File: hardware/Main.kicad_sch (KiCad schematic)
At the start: 16 parts, among them SW1 Bourns PEC11R, SW2 Bourns PEC11R, U3 RPi_Pico_TH

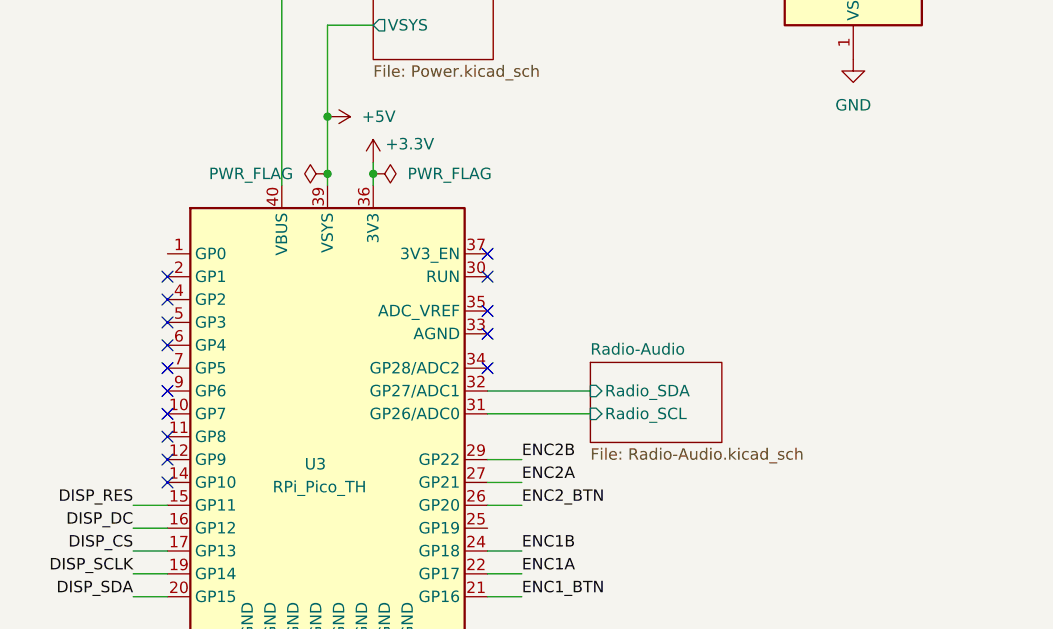
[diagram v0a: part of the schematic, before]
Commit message: PWM Audio, Power fix
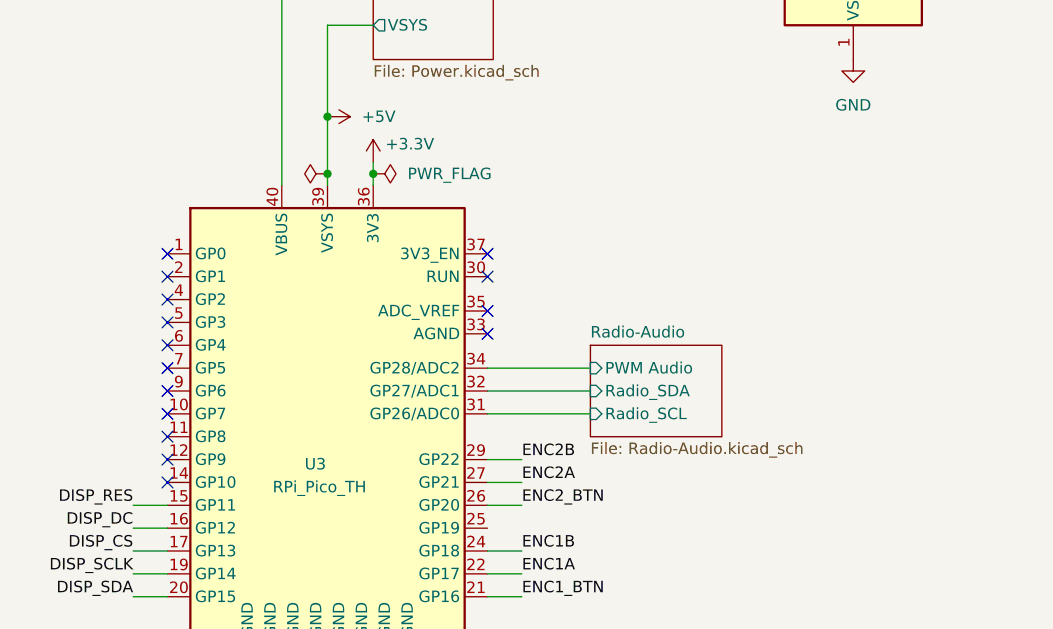
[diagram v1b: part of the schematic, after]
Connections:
- net Radio-Audio/PWM Audio: now reaches U3.34 (GP28/ADC2)
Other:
- sheet Radio-Audio ports: added PWM Audio; removed none
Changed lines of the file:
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@@
 	)
 	(no_connect
+		(at 105.41 78.74)
+	)
+	(no_connect
 		(at 105.41 99.06)
 	)
@@
 	)
 	(no_connect
-		(at 140.97 91.44)
-	)
-	(no_connect
 		(at 140.97 81.28)
 	)
@@
 	(wire
 		(pts
+			(xy 140.97 91.44) (xy 152.4 91.44)
+		)
+		(stroke
+			(width 0)
+			(type default)
+		)
+	)
+	(wire
+		(pts
 			(xy 54.61 69.85) (xy 54.61 73.66)
 		)
@@
 		(on_board yes)
 		(dnp no)
-		(fields_autoplaced yes)
 		(property "Reference" "#FLG01"
 			(at 121.285 69.85 0)
@@
 		)
 		(property "Value" "PWR_FLAG"
-			(at 119.38 69.8499 90)
+			(at 115.316 70.104 90)
 			(effects
 				(font
@@
 				)
 				(justify left)
+				(hide yes)
 			)
 		)
@@
 	)
 	(sheet
-		(at 152.4 90.805)
-		(size 14.605 8.89)
+		(at 152.4 88.9)
+		(size 14.605 10.16)
 		(exclude_from_sim no)
 		(in_bom yes)
@@
 		)
 		(property "Sheetname" "Radio-Audio"
-			(at 152.4 90.0934 0)
+			(at 152.4 88.1884 0)
 			(effects
 				(font
@@
 		)
 		(property "Sheetfile" "Radio-Audio.kicad_sch"
-			(at 152.4 100.2796 0)
+			(at 152.4 99.6446 0)
 			(effects
 				(font
@@
 			(effects
 				(font
+					(size 1.27 1.27)
+				)
+				(justify left)
+			)
+		)
+		(pin "PWM Audio" input
+			(at 152.4 91.44 180)
+			(effects
+				(font

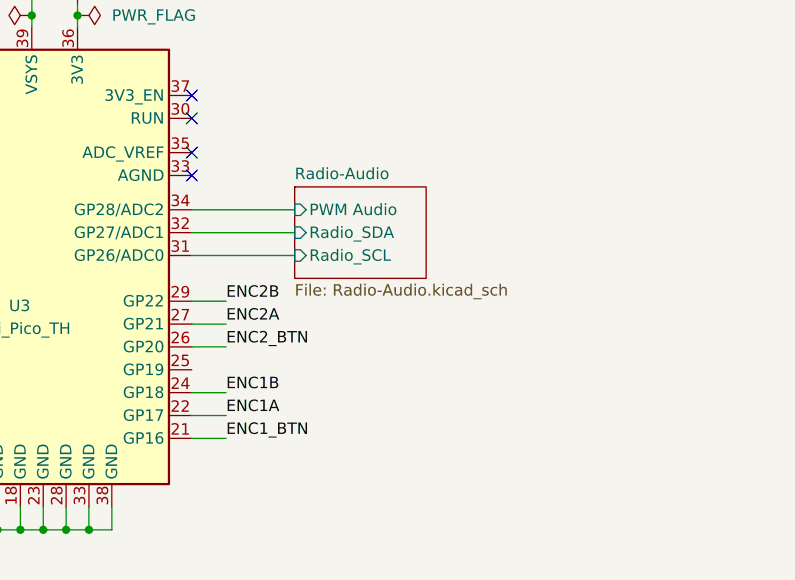
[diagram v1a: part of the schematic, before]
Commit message: Repositioned + Added volume potentiometer to PMW Audio
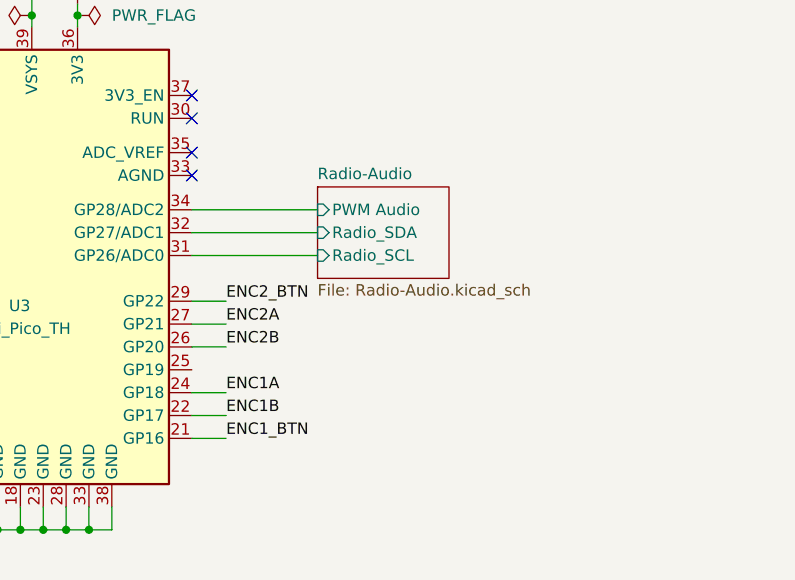
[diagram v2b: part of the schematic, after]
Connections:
- net ENC1A: now also U3.24 (GP18); no longer U3.22 (GP17)
- net ENC1B: now also U3.22 (GP17); no longer U3.24 (GP18)
- net ENC2B: now also U3.26 (GP20); no longer U3.29 (GP22)
- net ENC2_BTN: now also U3.29 (GP22); no longer U3.26 (GP20)
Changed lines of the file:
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@@
 	(wire
 		(pts
-			(xy 140.97 93.98) (xy 152.4 93.98)
+			(xy 140.97 93.98) (xy 154.94 93.98)
 		)
 		(stroke
@@
 	(wire
 		(pts
-			(xy 144.78 111.76) (xy 140.97 111.76)
+			(xy 144.78 114.3) (xy 140.97 114.3)
 		)
 		(stroke
@@
 	(wire
 		(pts
-			(xy 144.78 101.6) (xy 140.97 101.6)
+			(xy 144.78 106.68) (xy 140.97 106.68)
 		)
 		(stroke
@@
 	(wire
 		(pts
-			(xy 144.78 114.3) (xy 140.97 114.3)
+			(xy 144.78 111.76) (xy 140.97 111.76)
 		)
 		(stroke
@@
 	(wire
 		(pts
-			(xy 140.97 96.52) (xy 152.4 96.52)
+			(xy 140.97 96.52) (xy 154.94 96.52)
 		)
 		(stroke
@@
 	(wire
 		(pts
-			(xy 140.97 106.68) (xy 144.78 106.68)
+			(xy 140.97 101.6) (xy 144.78 101.6)
 		)
 		(stroke
@@
 	(wire
 		(pts
-			(xy 140.97 91.44) (xy 152.4 91.44)
+			(xy 140.97 91.44) (xy 154.94 91.44)
 		)
 		(stroke
@@
 	)
 	(label "ENC1B"
-		(at 144.78 111.76 0)
+		(at 144.78 114.3 0)
 		(effects
 			(font
@@
 	)
 	(label "ENC2_BTN"
-		(at 144.78 106.68 0)
+		(at 144.78 101.6 0)
 		(effects
 			(font
@@
 	)
 	(label "ENC1A"
-		(at 144.78 114.3 0)
+		(at 144.78 111.76 0)
 		(effects
 			(font
@@
 	)
 	(label "ENC2B"
-		(at 144.78 101.6 0)
+		(at 144.78 106.68 0)
 		(effects
 			(font
@@
 	)
 	(sheet
-		(at 152.4 88.9)
+		(at 154.94 88.9)
 		(size 14.605 10.16)
 		(exclude_from_sim no)
@@
 		)
 		(property "Sheetname" "Radio-Audio"
-			(at 152.4 88.1884 0)
+			(at 154.94 88.1884 0)
 			(effects
 				(font
@@
 		)
 		(property "Sheetfile" "Radio-Audio.kicad_sch"
-			(at 152.4 99.6446 0)
+			(at 154.94 99.6446 0)
 			(effects
 				(font
@@
 		)
 		(pin "Radio_SDA" input
-			(at 152.4 93.98 180)
+			(at 154.94 93.98 180)
 			(effects
 				(font
@@
 		)
 		(pin "Radio_SCL" input
-			(at 152.4 96.52 180)
+			(at 154.94 96.52 180)
 			(effects
 				(font
@@
 		)
 		(pin "PWM Audio" input
-			(at 152.4 91.44 180)
+			(at 154.94 91.44 180)
 			(effects
 				(font

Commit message: Did it all lmao (pcb traces ready for full review)
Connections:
- net ENC2A: now also U3.32 (GP27/ADC1); no longer U3.27 (GP21)
- net ENC2B: now also U3.31 (GP26/ADC0); no longer U3.26 (GP20)
- net ENC2_BTN: now also U3.34 (GP28/ADC2); no longer U3.29 (GP22)
- net Radio-Audio/PWM Audio: now also U3.14 (GP10); no longer U3.34 (GP28/ADC2)
- net Radio-Audio/Radio_SCL: now also U3.12 (GP9); no longer U3.31 (GP26/ADC0)
- net Radio-Audio/Radio_SDA: now also U3.11 (GP8); no longer U3.32 (GP27/ADC1)
- no-connect marks 15 -> 16
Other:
- moved on the sheet: DISP1, U3

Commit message: Minor Changes
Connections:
- net ENC1A: now also U3.22 (GP17); no longer U3.24 (GP18)
- net ENC1B: now also U3.24 (GP18); no longer U3.22 (GP17)
